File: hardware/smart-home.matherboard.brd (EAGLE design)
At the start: 78 x 54 mm, 11 parts, among them J1 A2501WV-03P, J2 A2501WV-04P, U1 CC2652P2-DUOWEISI

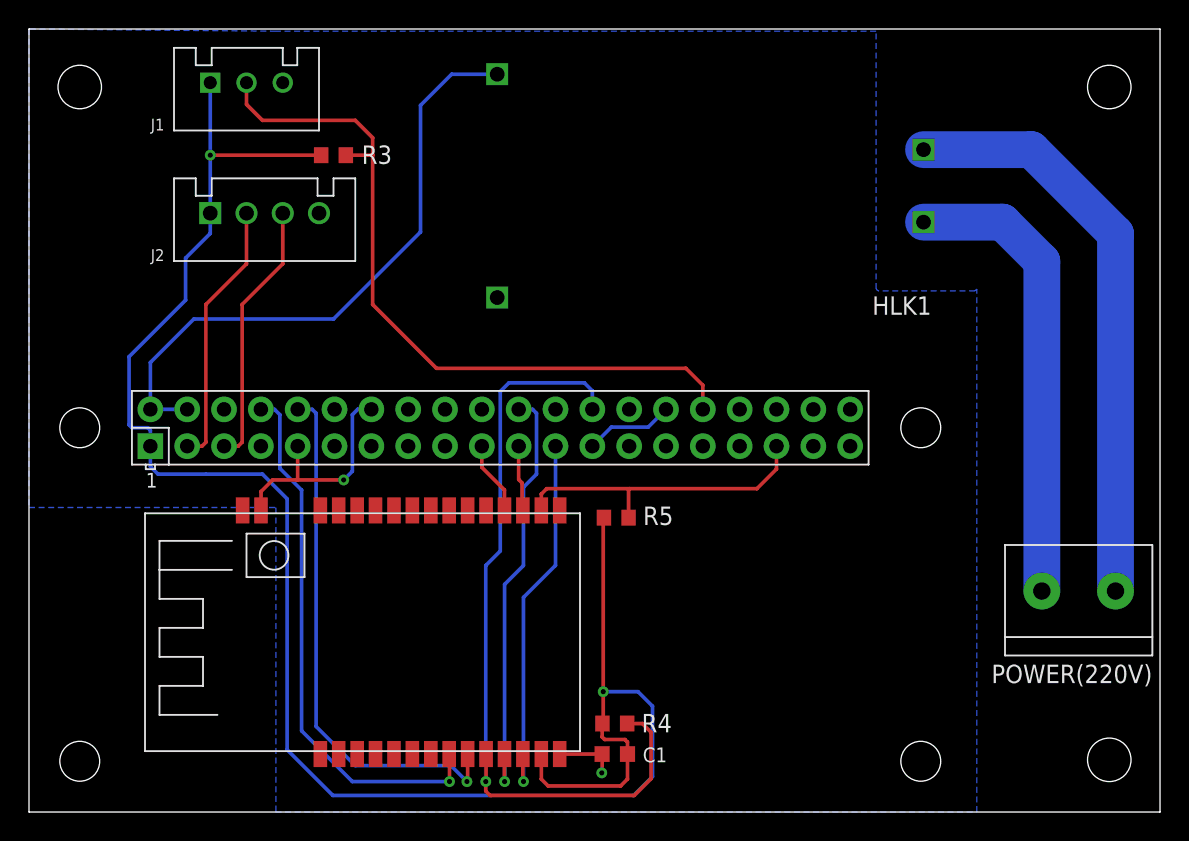
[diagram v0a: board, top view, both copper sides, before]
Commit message: Add buttons for reset and flash
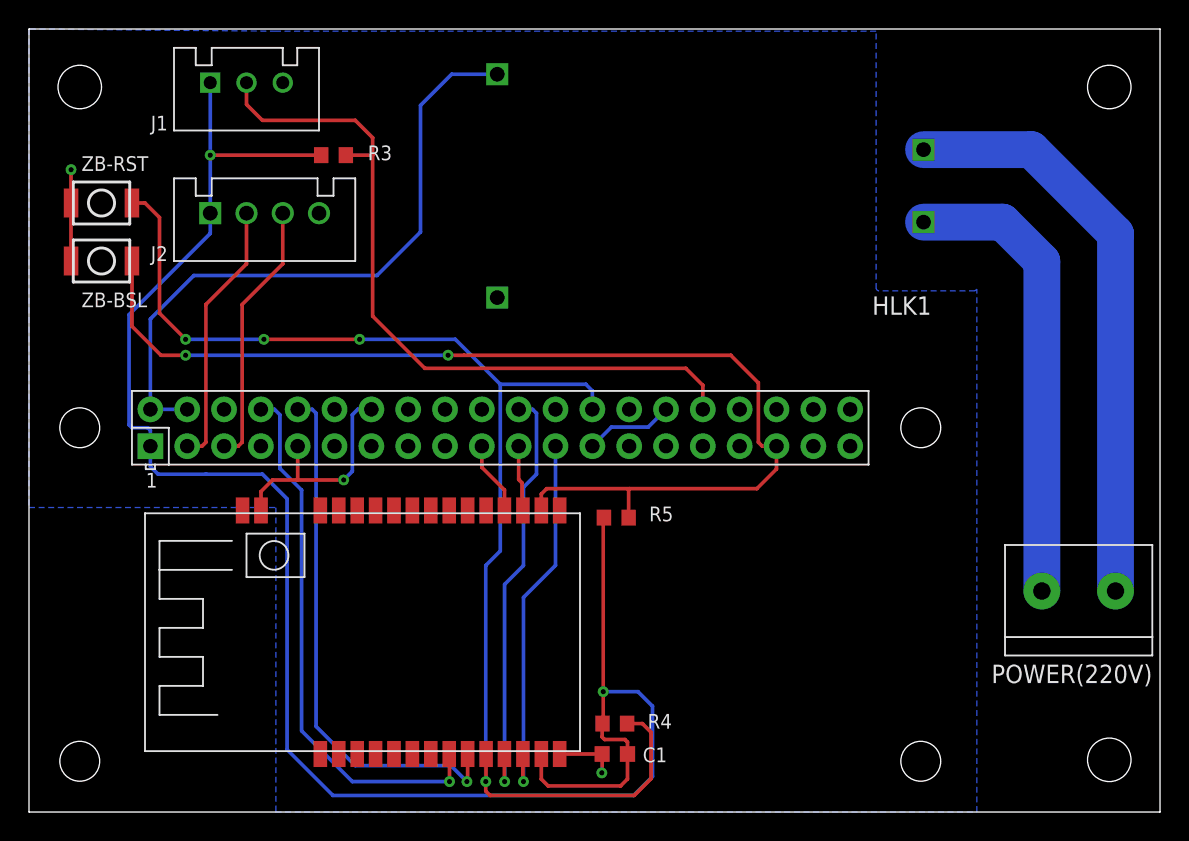
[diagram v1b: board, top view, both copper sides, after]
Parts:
- added ZB-BSL, ZB-RST: SKRKAEE020, switch:SKRKAEE020
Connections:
- net BSL_TRIGGER: now also ZB-BSL.2
- net GND: now also ZB-BSL.1, ZB-RST.1
- net JRES: now also ZB-RST.2
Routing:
- net BSL_TRIGGER: track 21.7 -> 76.4 mm, vias 0 -> 2
- net JRES: track 55.1 -> 89.7 mm, vias 1 -> 4
- net GND: track 26.3 -> 32.6 mm, vias 2 -> 3
- net +5V: track 43.0 -> 44.8 mm
